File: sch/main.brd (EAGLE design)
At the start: 50.5 x 49.5 mm, 39 parts

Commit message: [ update ] schematics, routing
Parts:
- CON_ANT: value (none) -> BU-SMA-G; device pinhead:1X02 -> con-coax:BU-SMA-G
- moved R12 5.08 mm to (19.1, 39.4), turned to 270 degrees
- moved R14 5.08 mm to (17.8, 39.4)
- moved R15 5.08 mm to (16.5, 39.4), turned to 270 degrees
- moved R16 5.08 mm to (15.2, 39.4), turned to 270 degrees
- moved R17 5.08 mm to (14.0, 39.4)
- moved R18 5.08 mm to (12.7, 39.4), turned to 270 degrees
- moved R19 5.08 mm to (11.4, 39.4)
- moved R20 5.08 mm to (10.2, 39.4), turned to 270 degrees
- moved R21 5.08 mm to (8.89, 39.4)
- moved R22 5.08 mm to (7.62, 39.4), turned to 270 degrees
- moved R23 5.08 mm to (6.35, 39.4)
- moved CON_POS 5.08 mm to (11.4, 35.6)
- moved R24 5.08 mm to (24.1, 36.8), turned to 270 degrees
- moved CON_ANT 2.54 mm to (25.4, 44.5), turned to 90 degrees
- moved R1 1.27 mm to (47.0, 38.1)
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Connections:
- net ANT: now also CON_ANT.2, CON_ANT.3, CON_ANT.4, CON_ANT.5; no longer CON_ANT.1
- net GND: now also CON_ANT.1; no longer CON_ANT.2
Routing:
- net SW_POS: track 14.0 -> 62.1 mm, vias 0 -> 2
- net VREG_33: track 65.7 -> 110.1 mm
- net SW_MODE: track 16.5 -> 49.3 mm, vias 0 -> 1
- net ANT: track 0.00 -> 28.3 mm
- net N$22: track 5.23 -> 2.39 mm
- net N$20: track 5.23 -> 2.39 mm
- net N$18: track 5.23 -> 2.39 mm
- net N$16: track 5.23 -> 2.39 mm
- net N$15: track 5.23 -> 2.39 mm
- net N$13: track 5.23 -> 2.39 mm
- net GND: track 24.4 -> 22.1 mm
- net VBAT_ON: track 25.9 -> 24.7 mm
- added copper zone on layer 16, net GND

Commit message: [ update ] schematics, routing
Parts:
- removed SW_MODE, SW_POS: 50-1POLE30, switch:50-1POLE30
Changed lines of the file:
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@@
 </class>
 </classes>
-<designrules name="default">
+<designrules name="SeeedStudio_DRU_no_angle_2layer">
 <description language="de">&lt;b&gt;EAGLE Design Rules&lt;/b&gt;
 &lt;p&gt;
@@
 necessary adjustments and save your customized
 design rules under a new name.</description>
+<description language="zh">&lt;b&gt;Seeed Studio EAGLE Design Rules&lt;/b&gt;
+</description>
 <param name="layerSetup" value="(1*16)"/>
-<param name="mtCopper" value="0.035mm 0.035mm 0.035mm 0.035mm 0.035mm 0.035mm 0.035mm 0.035mm 0.035mm 0.035mm 0.035mm 0.035mm 0.035mm 0.035mm 0.035mm 0.035mm"/>
-<param name="mtIsolate" value="1.5mm 0.15mm 0.2mm 0.15mm 0.2mm 0.15mm 0.2mm 0.15mm 0.2mm 0.15mm 0.2mm 0.15mm 0.2mm 0.15mm 0.2mm"/>
-<param name="mdWireWire" value="8mil"/>
-<param name="mdWirePad" value="8mil"/>
-<param name="mdWireVia" value="8mil"/>
-<param name="mdPadPad" value="8mil"/>
-<param name="mdPadVia" value="8mil"/>
-<param name="mdViaVia" value="8mil"/>
-<param name="mdSmdPad" value="8mil"/>
-<param name="mdSmdVia" value="8mil"/>
-<param name="mdSmdSmd" value="8mil"/>
+<param name="mtCopper" value="0.035mm 0.0175mm 0.035mm 0.035mm 0.035mm 0.035mm 0.035mm 0.035mm 0.035mm 0.035mm 0.035mm 0.035mm 0.035mm 0.035mm 0.0175mm 0.035mm"/>
+<param name="mtIsolate" value="1.5mm 1.1mm 0.2mm 0.15mm 0.2mm 0.15mm 0.2mm 0.15mm 0.2mm 0.15mm 0.2mm 0.15mm 0.2mm 0.15mm 0.2mm"/>
+<param name="mdWireWire" value="6mil"/>
+<param name="mdWirePad" value="6mil"/>
+<param name="mdWireVia" value="6mil"/>
+<param name="mdPadPad" value="6mil"/>
+<param name="mdPadVia" value="6mil"/>
+<param name="mdViaVia" value="6mil"/>
+<param name="mdSmdPad" value="0mil"/>
+<param name="mdSmdVia" value="0mil"/>
+<param name="mdSmdSmd" value="0mil"/>
 <param name="mdViaViaSameLayer" value="8mil"/>
 <param name="mnLayersViaInSmd" value="2"/>
-<param name="mdCopperDimension" value="40mil"/>
-<param name="mdDrill" value="8mil"/>
+<param name="mdCopperDimension" value="10mil"/>
+<param name="mdDrill" value="10mil"/>
 <param name="mdSmdStop" value="0mil"/>
-<param name="msWidth" value="10mil"/>
-<param name="msDrill" value="24mil"/>
-<param name="msMicroVia" value="9.99mm"/>
+<param name="msWidth" value="6mil"/>
+<param name="msDrill" value="12mil"/>
+<param name="msMicroVia" value="12mil"/>
 <param name="msBlindViaRatio" value="0.5"/>
 <param name="rvPadTop" value="0.25"/>
@@
 <param name="rlMinPadBottom" value="10mil"/>
 <param name="rlMaxPadBottom" value="20mil"/>
-<param name="rlMinViaOuter" value="8mil"/>
+<param name="rlMinViaOuter" value="6mil"/>
 <param name="rlMaxViaOuter" value="20mil"/>
-<param name="rlMinViaInner" value="8mil"/>
+<param name="rlMinViaInner" value="6mil"/>
 <param name="rlMaxViaInner" value="20mil"/>
 <param name="rlMinMicroViaOuter" value="4mil"/>
@@
 <param name="psTop" value="-1"/>
 <param name="psBottom" value="-1"/>
-<param name="psFirst" value="-1"/>
+<param name="psFirst" value="0"/>
 <param name="psElongationLong" value="100"/>
 <param name="psElongationOffset" value="100"/>
 <param name="mvStopFrame" value="1"/>
 <param name="mvCreamFrame" value="0"/>
-<param name="mlMinStopFrame" value="4mil"/>
-<param name="mlMaxStopFrame" value="4mil"/>
+<param name="mlMinStopFrame" value="2mil"/>
+<param name="mlMaxStopFrame" value="2mil"/>
 <param name="mlMinCreamFrame" value="0mil"/>
 <param name="mlMaxCreamFrame" value="0mil"/>
-<param name="mlViaStopLimit" value="0mil"/>
+<param name="mlViaStopLimit" value="25mil"/>
 <param name="srRoundness" value="0"/>
 <param name="srMinRoundness" value="0mil"/>
@@
 <param name="checkAngle" value="0"/>
 <param name="checkFont" value="1"/>
-<param name="checkRestrict" value="1"/>
+<param name="checkRestrict" value="0"/>
 <param name="useDiameter" value="13"/>
 <param name="maxErrors" value="50"/>
@@
 <element name="R25" library="resistor" package="R1206" value="330" x="21.59" y="25.4" rot="R180"/>
 <element name="R26" library="resistor" package="R1206" value="330" x="21.59" y="22.86" rot="R180"/>
-<element name="SW_POS" library="switch" package="50-1POLE30" value="50-1POLE30" x="39.37" y="59.69"/>
 <element name="CON_MODE" library="pinhdr_13" package="PINHDR_13" value="PINHDR_13" x="39.37" y="41.91" rot="R270"/>
-<element name="SW_MODE" library="switch" package="50-1POLE30" value="50-1POLE30" x="11.43" y="59.69"/>
 <element name="CON_POS" library="pinhdr_13" package="PINHDR_13" value="PINHDR_13" x="11.43" y="35.56" rot="R270"/>
 <element name="CON_ANT" library="con-coax" package="BU-SMA-G" value="BU-SMA-G" x="25.4" y="44.45" rot="R90">

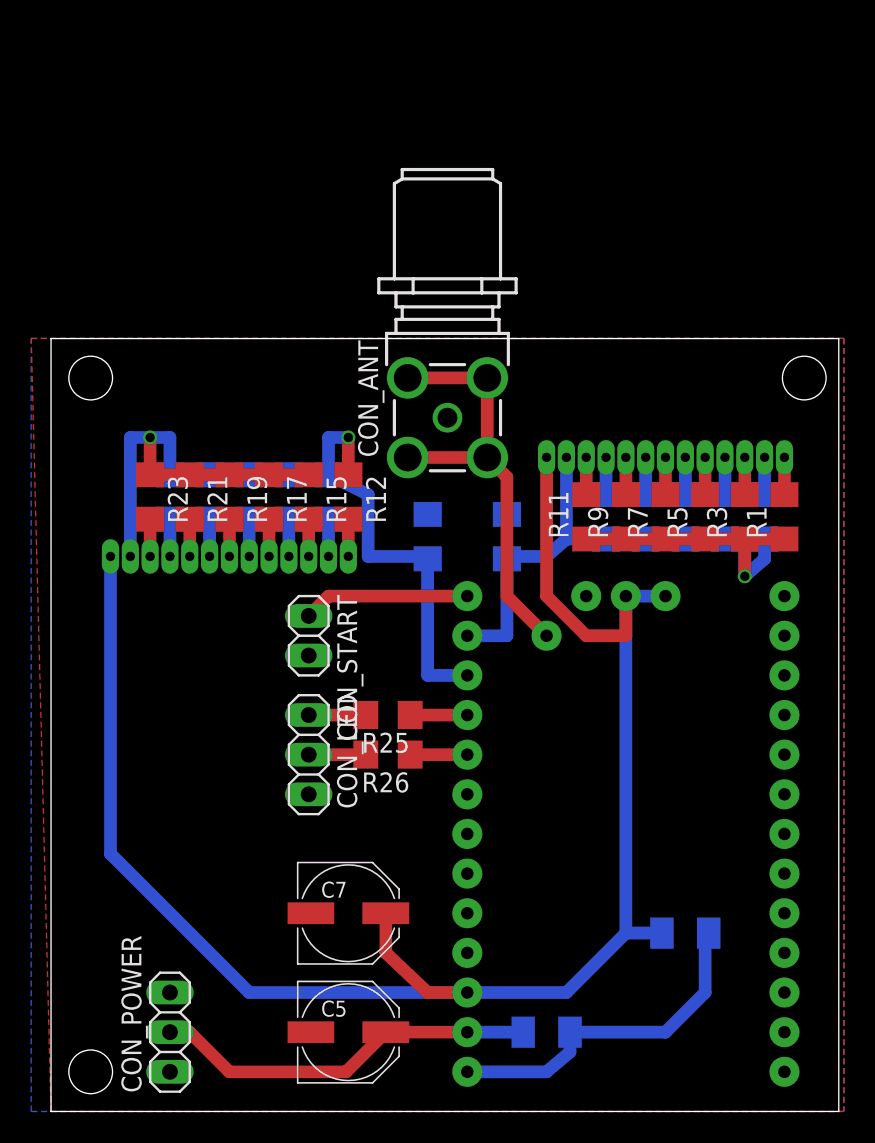
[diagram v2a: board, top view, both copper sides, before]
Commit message: [ update ] silkscreen cleaned
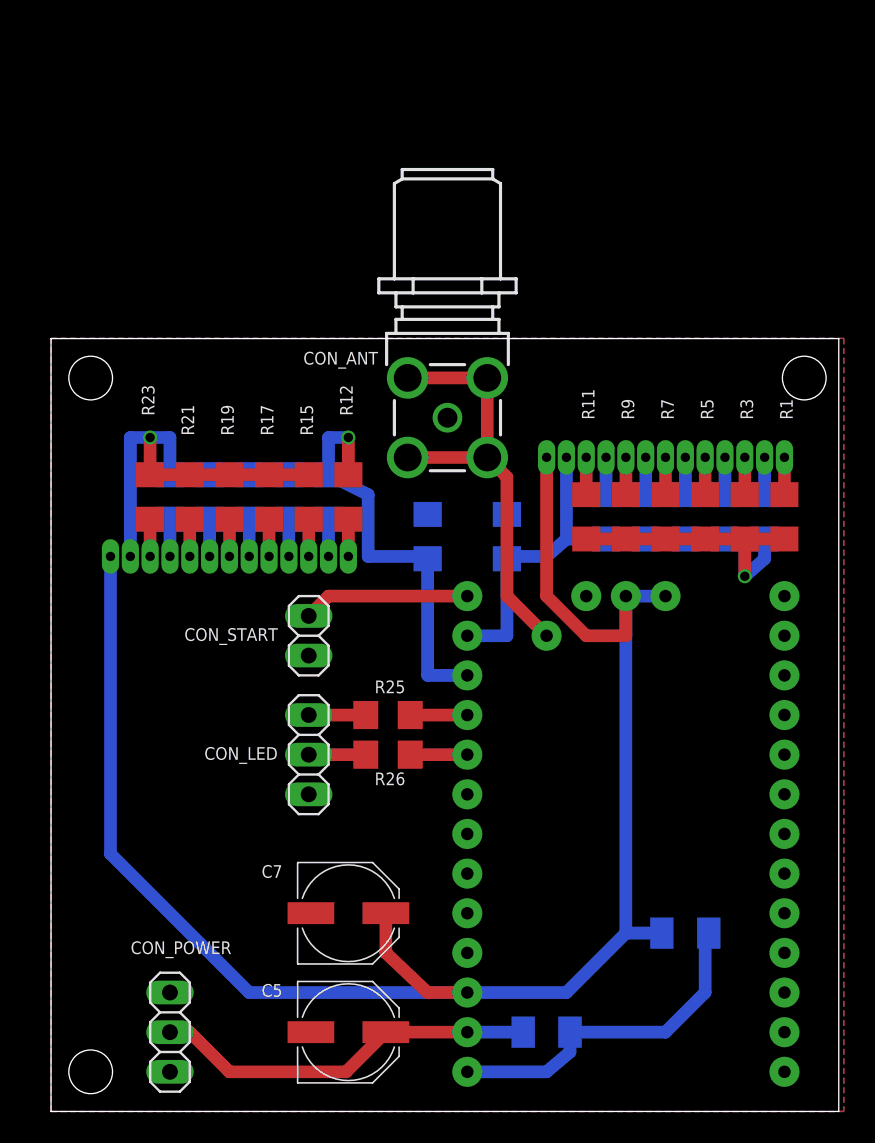
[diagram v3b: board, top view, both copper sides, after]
